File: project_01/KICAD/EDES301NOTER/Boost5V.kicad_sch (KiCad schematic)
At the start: 9 parts, among them Q2 BSS84, U3 TPS613222ADBVR

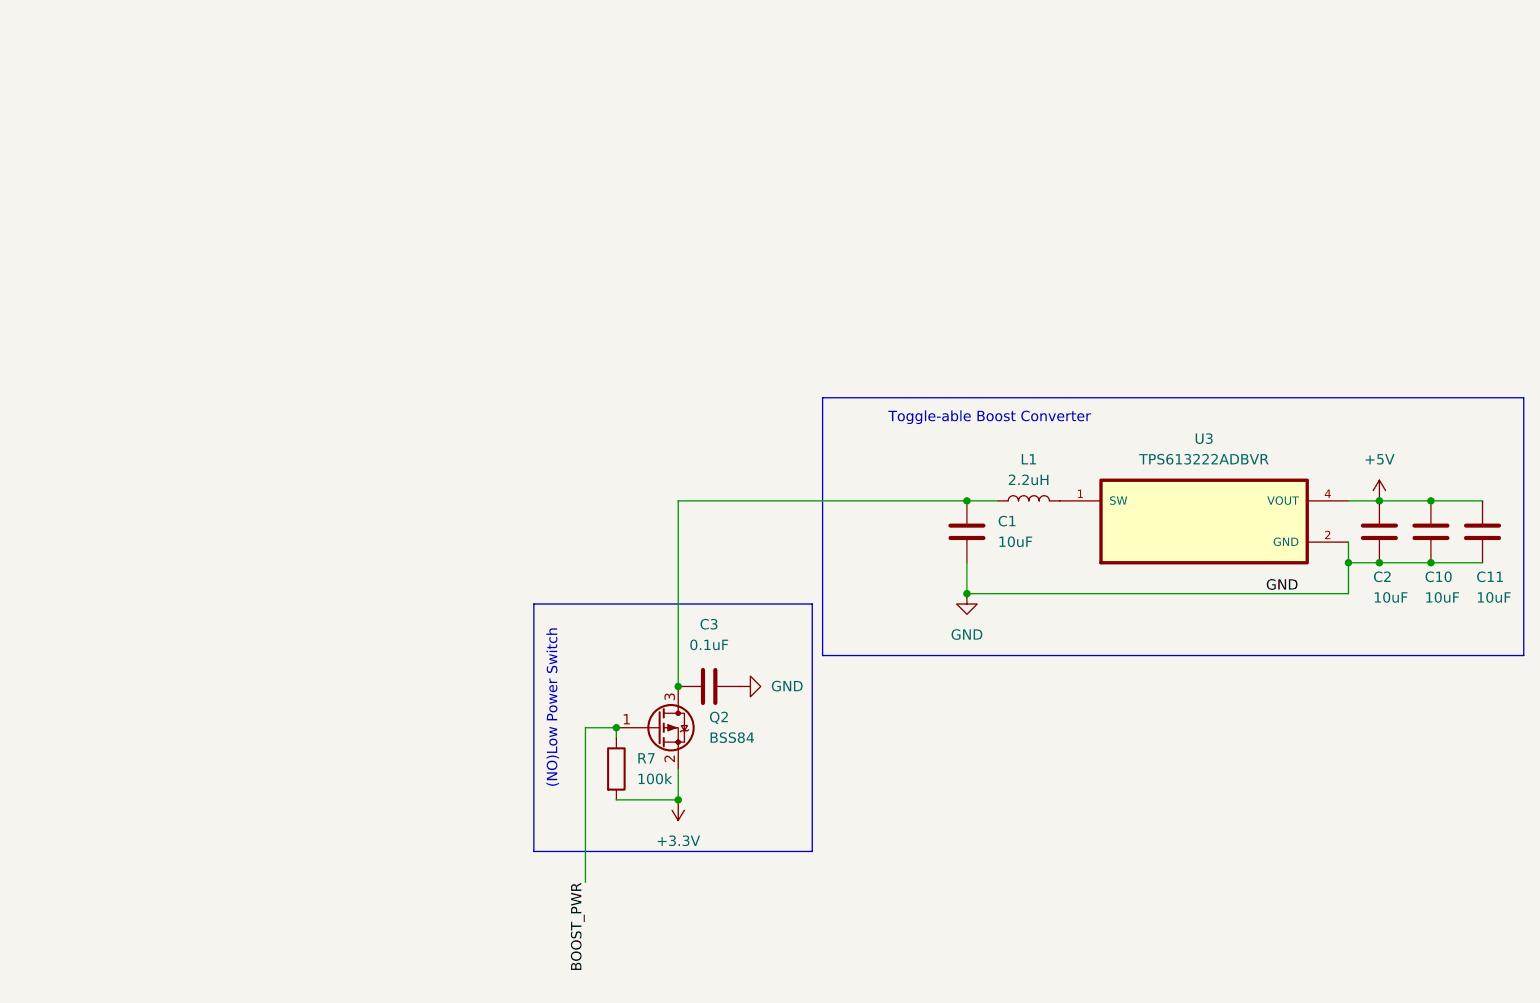
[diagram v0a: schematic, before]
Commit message: Revise Boost5V schematic and add STIKE symbols
Refactor Boost5V.kicad_sch: updated title block and paper size, reorganized and renamed many symbol definitions (capacitor/inductor/diode/resistor/LED/driver), adjusted pin assignments, footprints, datasheet links and symbol graphics. Added new STIKE-related schematic symbols (Slide Switch, LipoConnection) and multiple KiCad footprint/symbol files under KICAD Files. Added project backup zips and freerouting.dsn, removed a temporary .kicad_sch.lck, and updated project metadata files (.kicad_pcb, .kicad_prl, .kicad_pro, .kicad_sch).
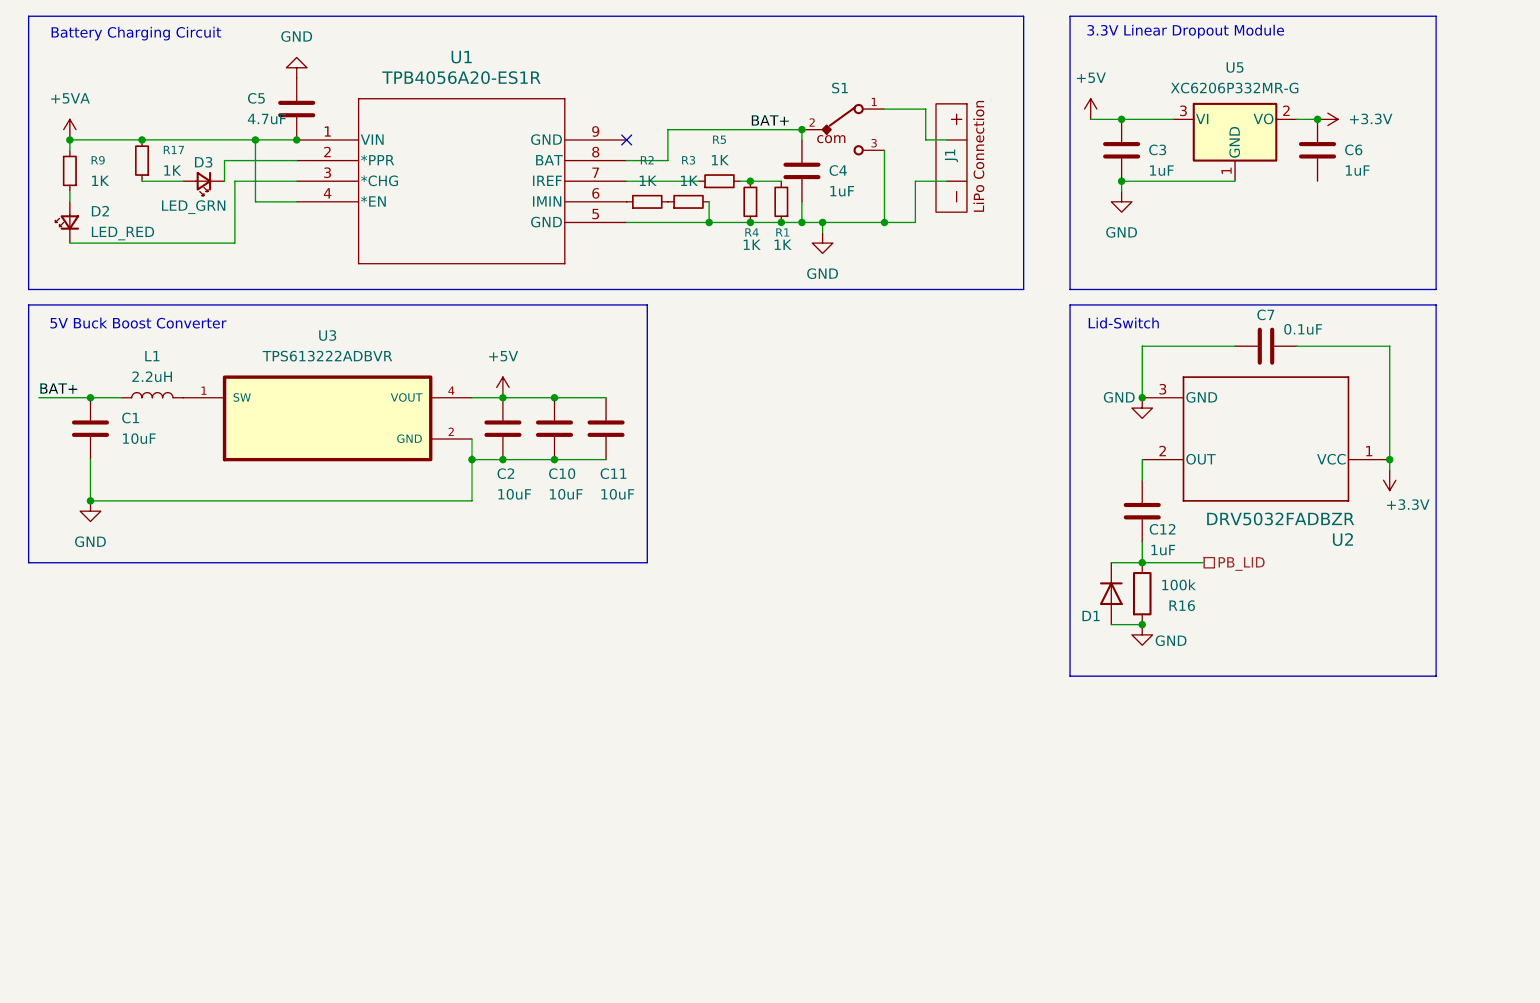
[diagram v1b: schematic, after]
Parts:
- removed Q2: BSS84, Package_TO_SOT_SMD:SOT-23, symbol Transistor_FET:BSS84
- removed R7: 100k, Footprints:RESC1607X60N, symbol Device:R
- added C12, C4, C6: 1uF, Capacitor_SMD:C_0603_1608Metric_Pad1.08x0.95mm_HandSolder, symbol Device:C
- added C5: 4.7uF, Capacitor_SMD:C_0603_1608Metric_Pad1.08x0.95mm_HandSolder, symbol Device:C
- added C7: 0.1uF, Capacitor_SMD:C_0603_1608Metric_Pad1.08x0.95mm_HandSolder, symbol Device:C
- added D1: BAT41ZFILM, Diode_SMD:D_SOD-123, symbol Device:D
- added D2: LED_RED, Diode_SMD:D_0603_1608Metric_Pad1.05x0.95mm_HandSolder, symbol Device:LED_Small
- added D3: LED_GRN, Diode_SMD:D_0603_1608Metric_Pad1.05x0.95mm_HandSolder, symbol Device:LED_Small
- added J1: ~, STIKE:LipoConnection, symbol STIKE:LipoConnection
- added R1, R17, R2, R3, R4, R5, R9: 1K, Resistor_SMD:R_0603_1608Metric_Pad0.98x0.95mm_HandSolder, symbol Device:R_Small
- added R16: 100k, Resistor_SMD:R_0603_1608Metric_Pad0.98x0.95mm_HandSolder, symbol Device:R
- added S1: ~, STIKE:450404015514, symbol STIKE:Slide Switch
- added U1: TPB4056A20-ES1R, STIKE:TPB4056A20-ES1R, symbol STIKE:TPB4056A20-ES1R
- added U2: DRV5032FADBZR, Package_TO_SOT_SMD:SOT-23-3, symbol DRV5032FCDBZR:DRV5032FCDBZR
- added U5: XC6206P332MR-G, Package_TO_SOT_SMD:TSOT-23, symbol STIKE:XC6206P332MR-G
- C1, C10, C11, C2: footprint Footprints:CAPC1608X90N -> Capacitor_SMD:C_0603_1608Metric_Pad1.08x0.95mm_HandSolder
- C3: value 0.1uF -> 1uF; footprint Footprints:CAPC1608X90 -> Capacitor_SMD:C_0603_1608Metric_Pad1.08x0.95mm_HandSolder
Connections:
- net +3.3V: now also C6.1, C7.1, U2.1 (VCC), U5.2 (VO)
- net +5V: now also C3.1, U5.3 (VI)
- net GND: now also C4.2, C5.1, C7.2, D1.2 (A), J1.2 (Batt_GND), R1.1, R16.2, R3.2, R4.1, S1.3, U1.5 (GND), U2.3 (GND), U5.1 (GND)
- net BAT+: now reaches C1.1, L1.1
- net BAT+: now also C4.1, S1.2, U1.8 (BAT); no longer C3.1
- new net: D3.1 (K), U1.2 (*PPR)
- new net: D3.2 (A), R17.1
- new net: J1.1 (Batt_Pos), S1.1
- new net: R5.1, U1.7 (IREF)
- new net: R1.2, R4.2, R5.2
- new net: D2.2 (A), R9.1
- new net: D2.1 (K), U1.3 (*CHG)
- new net: R2.1, U1.6 (IMIN)
- new net: R2.2, R3.1
- new net  : C12.1, U2.2 (OUT)
- new net +5VA: C5.2, R17.2, R9.2, U1.1 (VIN), U1.4 (*EN)
- new net PB_LID: C12.2, D1.1 (K), R16.1
- no-connect marks 0 -> 1
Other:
- note added: "3.3V Linear Dropout Module"
- note added: "5V Buck Boost Converter"
- note added: "Battery Charging Circuit"
- note added: "Lid-Switch"
- note removed: "(NO)Low Power Switch"
- note removed: "Toggle-able Boost Converter"
- title: 3.3V to 5V Boost Converter -> STIK eNote
- moved on the sheet: C1, C10, C11, C2, L1, U3
